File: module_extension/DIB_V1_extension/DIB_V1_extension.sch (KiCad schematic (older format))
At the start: 10 parts, among them J1 20-pin power socket, J3 28-pin module socket, J3 PROBE, J4 CABLE

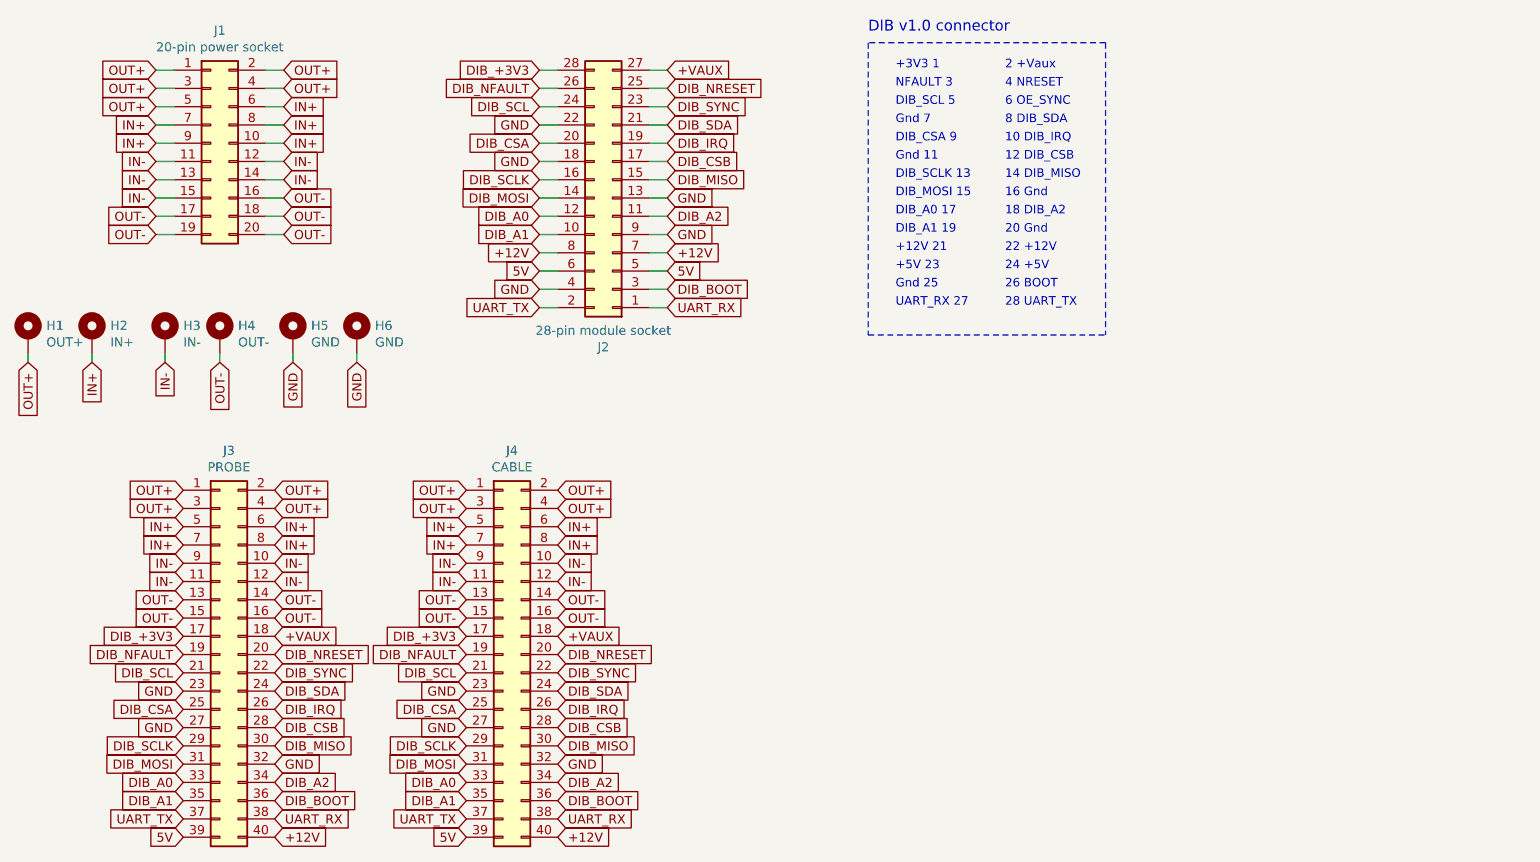
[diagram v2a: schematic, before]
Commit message: Changing pinout fix #3 fix #1
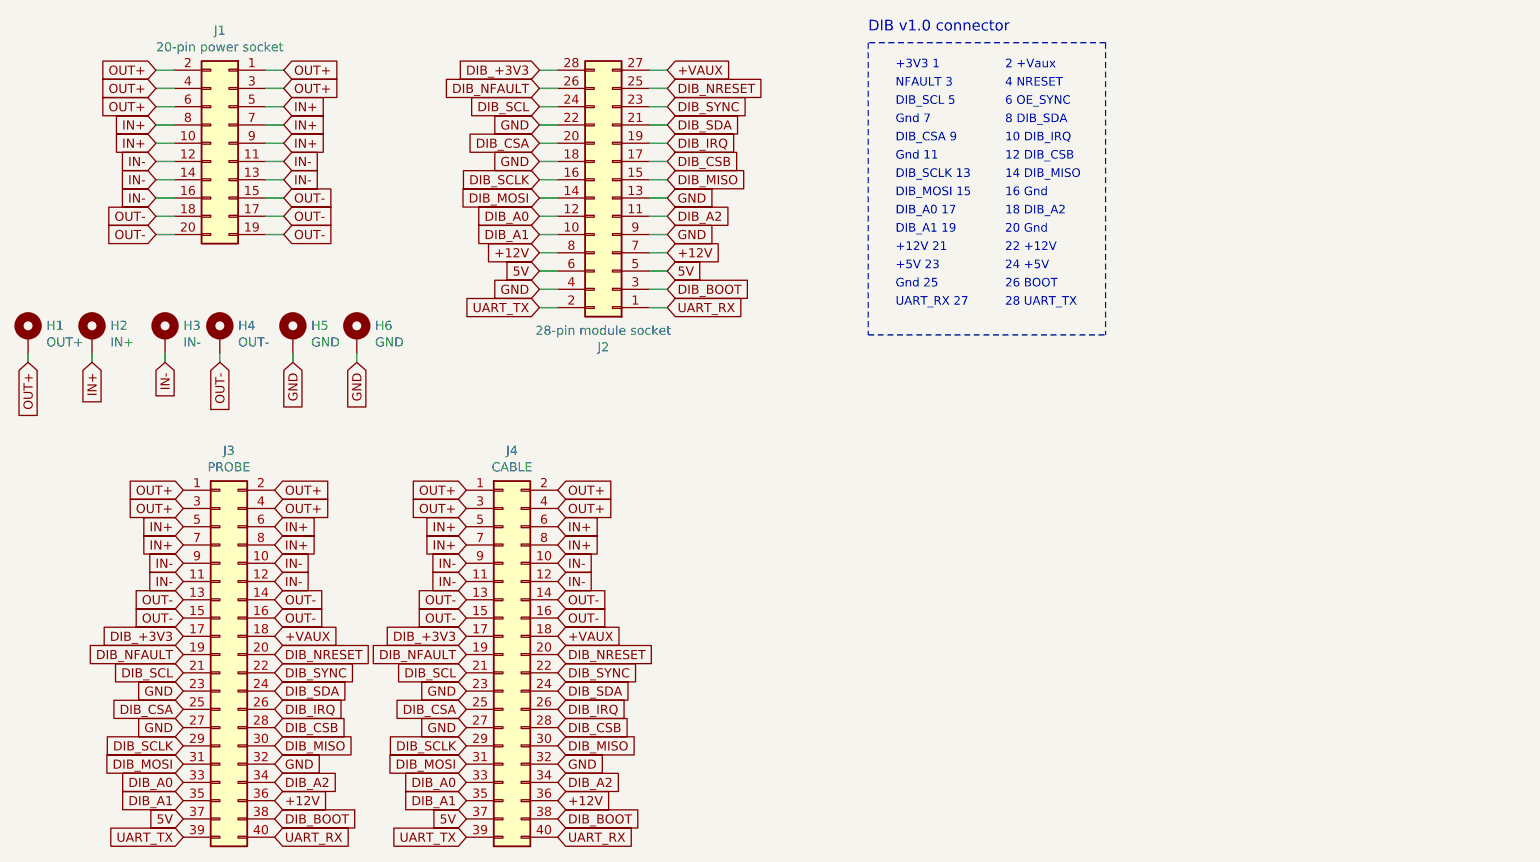
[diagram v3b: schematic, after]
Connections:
- net +12V: now also J3.36 (Pin_36), J4.36 (Pin_36); no longer J3.40 (Pin_40), J4.40 (Pin_40)
- net 5V: now also J3.37 (Pin_37), J4.37 (Pin_37); no longer J3.39 (Pin_39), J4.39 (Pin_39)
- net DIB_BOOT: now also J3.38 (Pin_38), J4.38 (Pin_38); no longer J3.36 (Pin_36), J4.36 (Pin_36)
- net IN+: now also J1.5 (Pin_5); no longer J1.6 (Pin_6)
- net IN-: now also J1.16 (Pin_16); no longer J1.15 (Pin_15)
- net OUT+: now also J1.6 (Pin_6); no longer J1.5 (Pin_5)
- net OUT-: now also J1.15 (Pin_15); no longer J1.16 (Pin_16)
- net UART_RX: now also J3.40 (Pin_40), J4.40 (Pin_40); no longer J3.38 (Pin_38), J4.38 (Pin_38)
- net UART_TX: now also J3.39 (Pin_39), J4.39 (Pin_39); no longer J3.37 (Pin_37), J4.37 (Pin_37)
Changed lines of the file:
@@
 L Connector_Generic:Conn_02x10_Odd_Even J1
 U 1 1 5E22CB95
-P 1800 1450
-F 0 "J1" H 1850 2067 50  0000 C CNN
-F 1 "20-pin power socket" H 1850 1976 50  0000 C CNN
-F 2 "Connector_PinSocket_2.54mm:PinSocket_2x10_P2.54mm_Horizontal" H 1800 1450 50  0001 C CNN
-F 3 "~" H 1800 1450 50  0001 C CNN
-	1    1800 1450
-	1    0    0    -1
+P 1900 1450
+F 0 "J1" H 1950 2067 50  0000 C CNN
+F 1 "20-pin power socket" H 1950 1976 50  0000 C CNN
+F 2 "Connector_PinSocket_2.54mm:PinSocket_2x10_P2.54mm_Horizontal" H 1900 1450 50  0001 C CNN
+F 3 "~" H 1900 1450 50  0001 C CNN
+	1    1900 1450
+	-1   0    0    -1
 $EndComp
 Text GLabel 1500 1050 0    50   Input ~ 0
@@
 Text GLabel 3700 4950 2    50   Input ~ 0
 DIB_A2
+Text GLabel 2150 5150 2    50   Input ~ 0
+DIB_BOOT
+Text GLabel 2150 5250 2    50   Input ~ 0
+UART_RX
 Text GLabel 2150 5050 2    50   Input ~ 0
-DIB_BOOT
-Text GLabel 2150 5150 2    50   Input ~ 0
-UART_RX
-Text GLabel 2150 5250 2    50   Input ~ 0
 +12V
+Text GLabel 1650 5150 0    50   Input ~ 0
+5V
 Text GLabel 1650 5250 0    50   Input ~ 0
-5V
-Text GLabel 1650 5150 0    50   Input ~ 0
 UART_TX
 Text GLabel 3200 5050 0    50   Input ~ 0
@@
 Text GLabel 2150 4250 2    50   Input ~ 0
 DIB_NRESET
+Text GLabel 3700 5150 2    50   Input ~ 0
+DIB_BOOT
+Text GLabel 3200 5250 0    50   Input ~ 0
+UART_TX
+Text GLabel 3700 5250 2    50   Input ~ 0
+UART_RX
+Text GLabel 3200 5150 0    50   Input ~ 0
+5V
 Text GLabel 3700 5050 2    50   Input ~ 0
-DIB_BOOT
-Text GLabel 3200 5150 0    50   Input ~ 0
-UART_TX
-Text GLabel 3700 5150 2    50   Input ~ 0
-UART_RX
-Text GLabel 3200 5250 0    50   Input ~ 0
-5V
-Text GLabel 3700 5250 2    50   Input ~ 0
 +12V
 $EndSCHEMATC

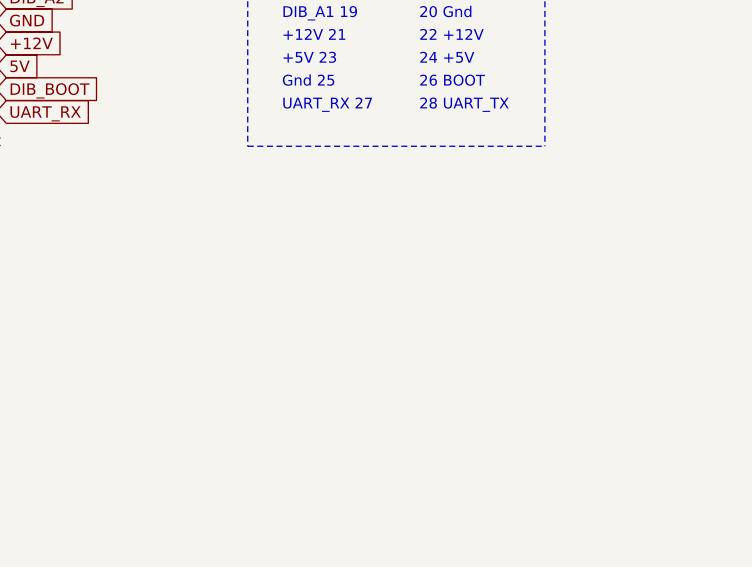
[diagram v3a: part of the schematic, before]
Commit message: Routing, adding mounting holesFix #2
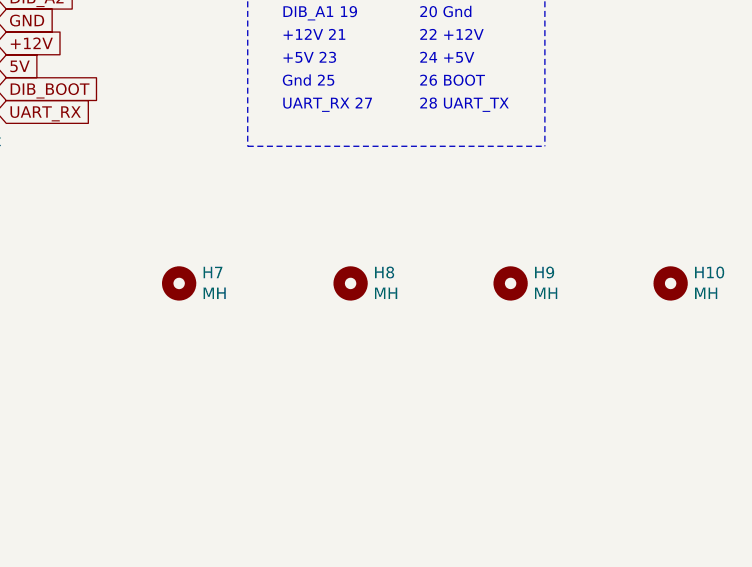
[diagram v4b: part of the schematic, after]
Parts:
- added H10, H7, H8, H9: MH, MountingHole:MountingHole_3.2mm_M3, symbol Mechanical:MountingHole
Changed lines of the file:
@@
 Text GLabel 3700 5050 2    50   Input ~ 0
 +12V
+$Comp
+L Mechanical:MountingHole H7
+U 1 1 5FEF1758
+P 5100 3100
+F 0 "H7" H 5200 3146 50  0000 L CNN
+F 1 "MH" H 5200 3055 50  0000 L CNN
+F 2 "MountingHole:MountingHole_3.2mm_M3" H 5100 3100 50  0001 C CNN
+F 3 "~" H 5100 3100 50  0001 C CNN
+	1    5100 3100
+	1    0    0    -1
+$EndComp
+$Comp
+L Mechanical:MountingHole H8
+U 1 1 5FEF1D77
+P 5850 3100
+F 0 "H8" H 5950 3146 50  0000 L CNN
+F 1 "MH" H 5950 3055 50  0000 L CNN
+F 2 "MountingHole:MountingHole_3.2mm_M3" H 5850 3100 50  0001 C CNN
+F 3 "~" H 5850 3100 50  0001 C CNN
+	1    5850 3100
+	1    0    0    -1
+$EndComp
+$Comp
+L Mechanical:MountingHole H9
+U 1 1 5FEF25E6
+P 6550 3100
+F 0 "H9" H 6650 3146 50  0000 L CNN
+F 1 "MH" H 6650 3055 50  0000 L CNN
+F 2 "MountingHole:MountingHole_3.2mm_M3" H 6550 3100 50  0001 C CNN
+F 3 "~" H 6550 3100 50  0001 C CNN
+	1    6550 3100
+	1    0    0    -1
+$EndComp
+$Comp
+L Mechanical:MountingHole H10
+U 1 1 5FEF2CD5
+P 7250 3100
+F 0 "H10" H 7350 3146 50  0000 L CNN
+F 1 "MH" H 7350 3055 50  0000 L CNN
+F 2 "MountingHole:MountingHole_3.2mm_M3" H 7250 3100 50  0001 C CNN
+F 3 "~" H 7250 3100 50  0001 C CNN
+	1    7250 3100
+	1    0    0    -1
+$EndComp
 $EndSCHEMATC
